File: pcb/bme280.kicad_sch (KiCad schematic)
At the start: 7 parts, among them J13 I2C Board, J14 I2C Sensor, U9 BME280

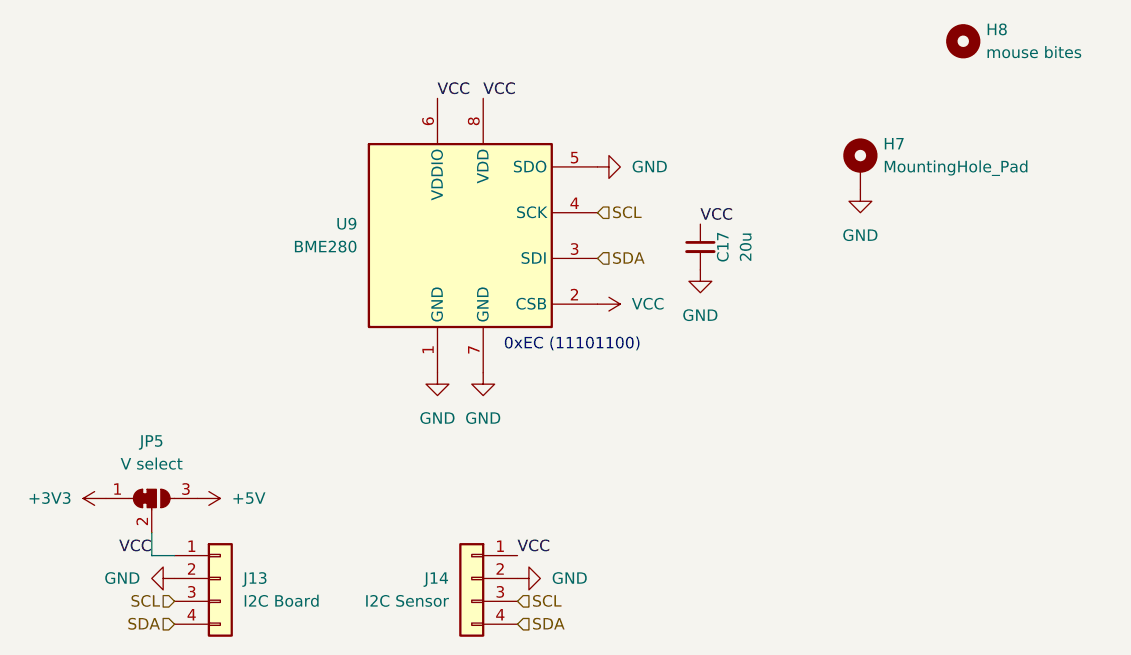
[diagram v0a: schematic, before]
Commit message: Rename pcb, add sensors and fix some issues
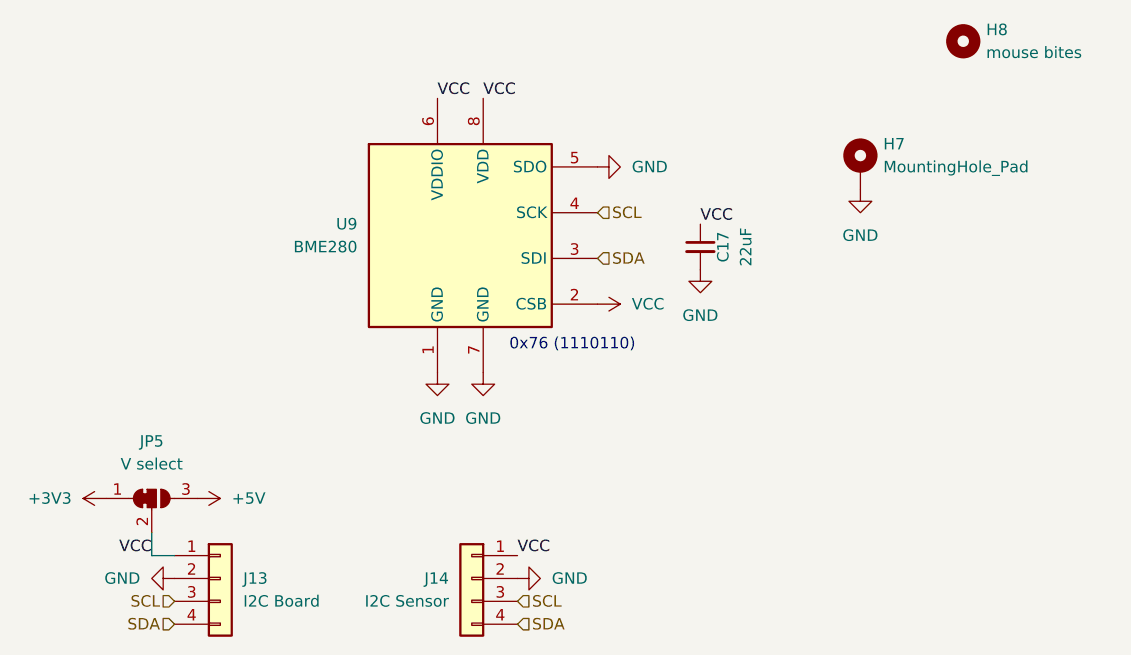
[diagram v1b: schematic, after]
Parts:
- C17: value 20u -> 22uF
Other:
- note added: "0x76 (1110110)"
- note removed: "0xEC (11101100)"
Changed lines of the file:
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@@
 		)
 	)
-	(text "0xEC (11101100)"
+	(text "0x76 (1110110)"
 		(exclude_from_sim no)
 		(at 83.566 78.232 0)
@@
 			)
 		)
-		(property "Value" "20u"
+		(property "Value" "22uF"
 			(at 102.87 67.31 90)
 			(effects
